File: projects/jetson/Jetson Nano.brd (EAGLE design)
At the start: 120 x 100 mm, 20 parts

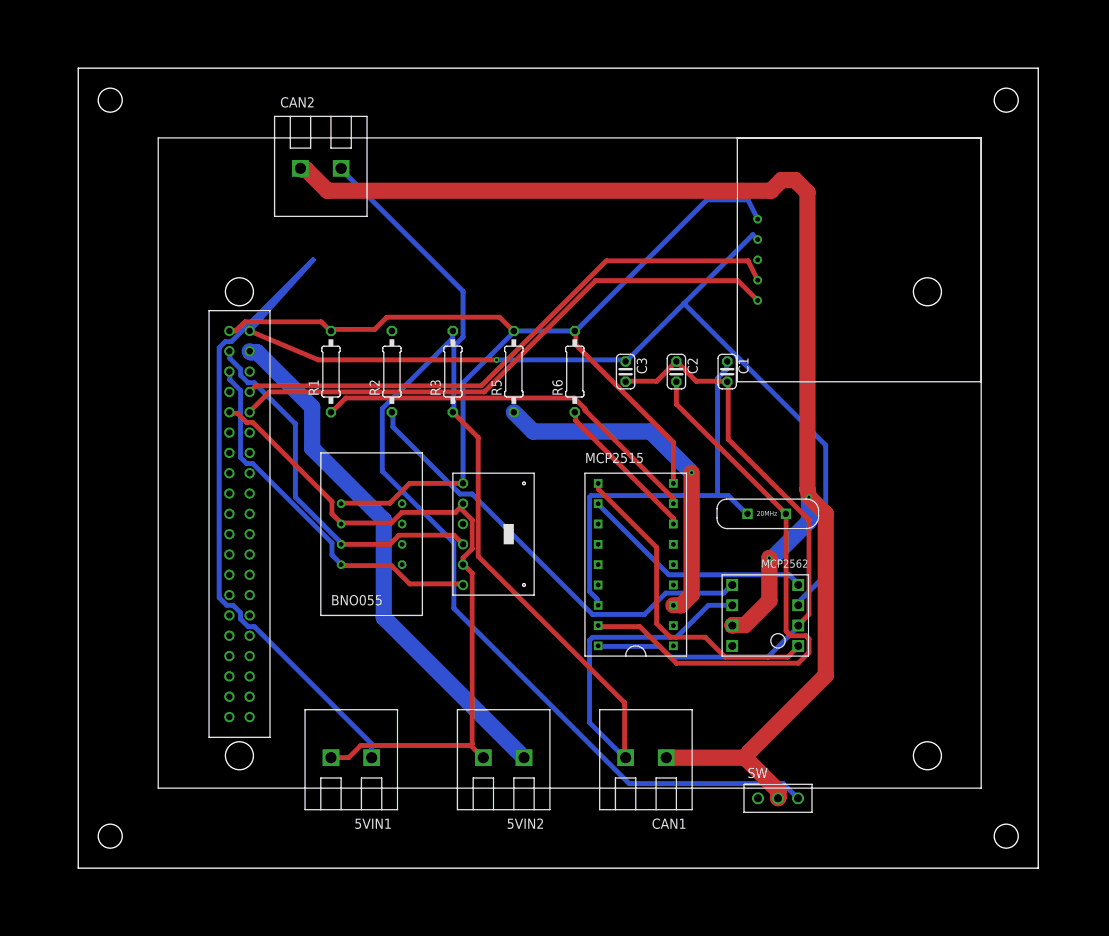
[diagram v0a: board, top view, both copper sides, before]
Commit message: Autoroute Jetson Board
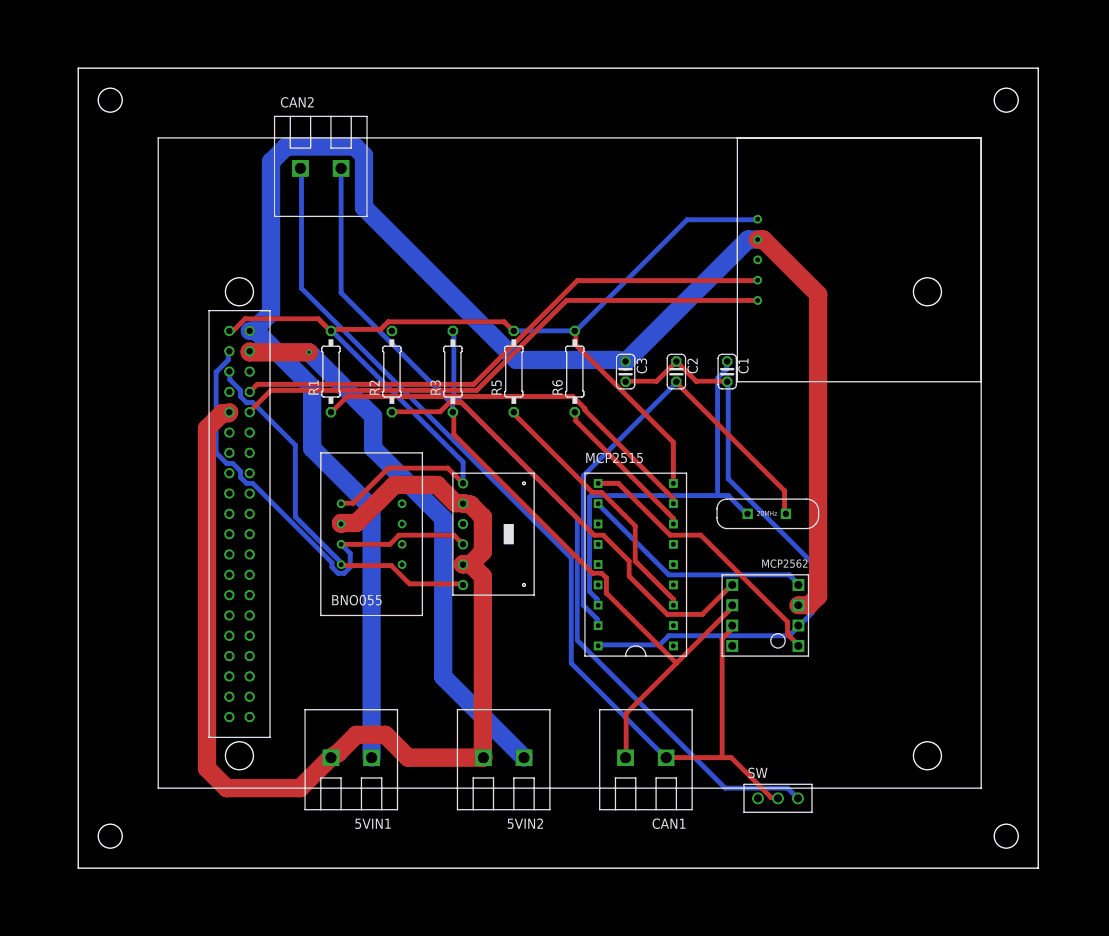
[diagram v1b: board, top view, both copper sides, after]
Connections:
- net +5V renamed +5V_1
- net N$2 renamed GND_1
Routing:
- net CAN_H2: track 179.2 -> 125.7 mm, vias 2 -> 0
- net GND_1: track 88.8 -> 139.4 mm
- net N$16: track 125.8 -> 104.6 mm
- net N$15: track 94.9 -> 80.9 mm
- net N$7: track 70.7 -> 58.4 mm
- net CAN_INT: track 43.4 -> 33.1 mm, vias 1 -> 0
- net N$3: track 46.7 -> 57.0 mm
- net +5V_1: track 205.9 -> 215.8 mm, vias 1 -> 0
- net N$8: track 40.7 -> 34.4 mm
- net 5V_2: track 65.5 -> 69.4 mm, vias 0 -> 1
- net +3V3: track 138.9 -> 142.2 mm
- net N$11: track 71.8 -> 69.3 mm
- net N$12: track 71.4 -> 69.3 mm
- net N$14: track 55.5 -> 56.6 mm
- net V-: track 77.4 -> 76.6 mm

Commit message: wakuwaku
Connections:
- removed net GND_1: 5VIN1.P$2, 5VIN2.P$2, JN1.GND-2, U$1.GND, U$1.SDO, U$2.2_GND
- removed net V-: C1.2, C2.1, C3.2, MCP1.VSS, U$4.VSS
- new net GND: 5VIN1.P$2, 5VIN2.P$2, C1.2, C2.1, C3.2, JN1.GND-2, MCP1.VSS, U$1.GND, U$1.SDO, U$2.2_GND, U$3.GND, U$4.VSS
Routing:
- net GND: track 0.00 -> 265.1 mm, vias 0 -> 1
- net GND_1: track 139.4 -> 0.00 mm
- net V-: track 76.6 -> 0.00 mm
- net N$8: track 34.4 -> 45.3 mm
- net N$3: track 57.0 -> 46.5 mm
- net CAN_H2: track 125.7 -> 136.0 mm
- net N$16: track 104.6 -> 113.6 mm
- net +5V_1: track 215.8 -> 207.7 mm
- net N$12: track 69.3 -> 75.7 mm, vias 0 -> 1
- net 5V_2: track 69.4 -> 66.5 mm, vias 1 -> 0
- net N$14: track 56.6 -> 54.5 mm
- net N$4: track 46.8 -> 48.6 mm
- net +3V3: track 142.2 -> 140.5 mm
- net N$13: track 49.6 -> 49.0 mm
- net N$7: track 58.4 -> 58.3 mm, vias 0 -> 1
- added copper zone on layer 1, net GND
- added copper zone on layer 16, net GND

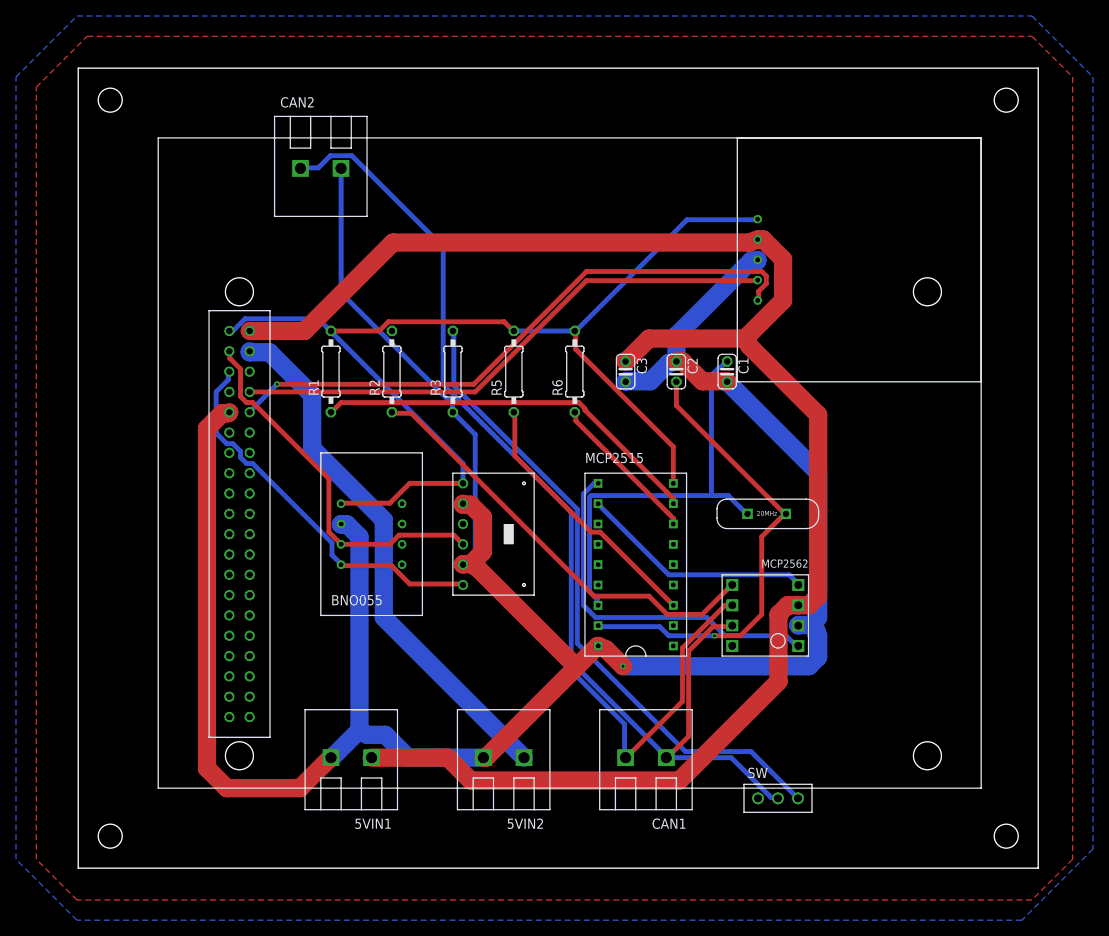
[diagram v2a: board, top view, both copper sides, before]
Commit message: Resize Jetson Board
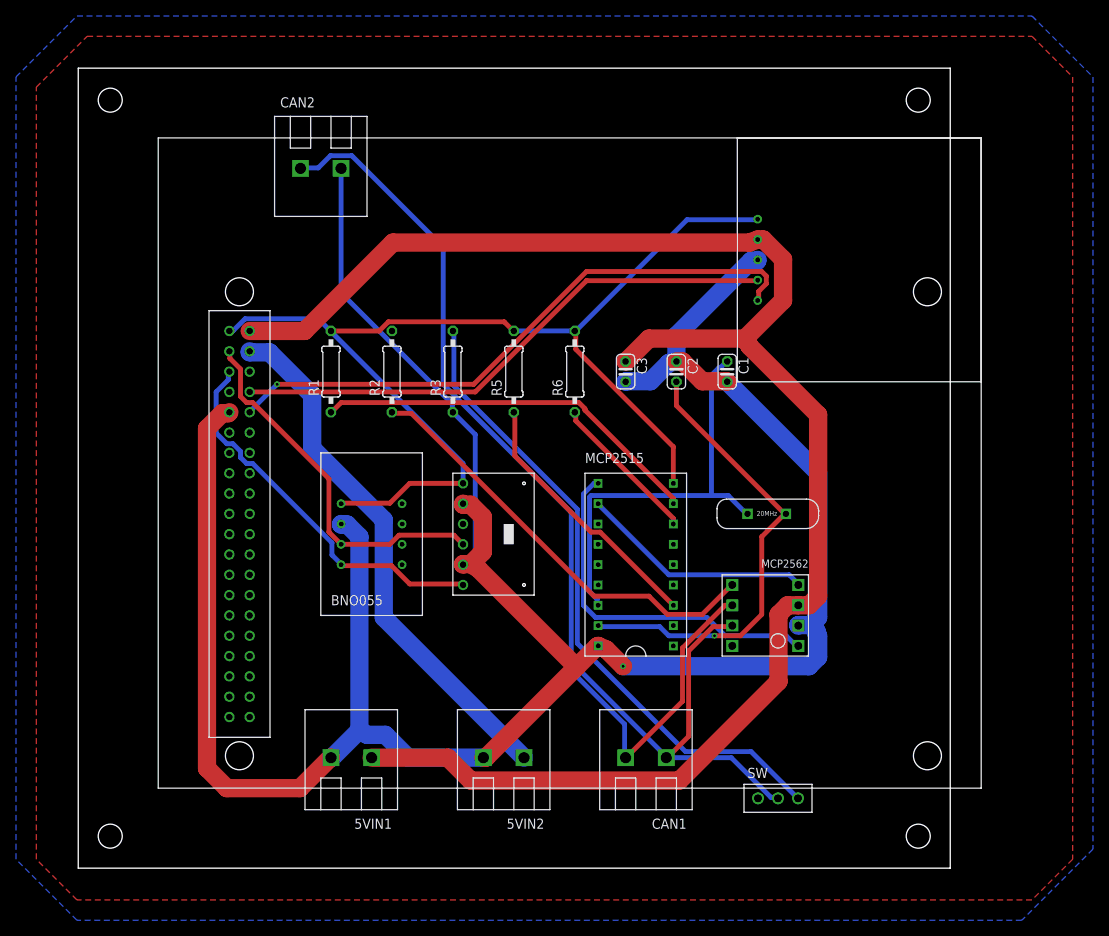
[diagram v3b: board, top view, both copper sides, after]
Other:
- board size 120 x 100 mm -> 109 x 100 mm
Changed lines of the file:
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@@
 <setting verticaltext="up"/>
 </settings>
-<grid distance="50" unitdist="mil" unit="mm" style="lines" multiple="1" display="no" altdistance="5" altunitdist="mil" altunit="mm"/>
+<grid distance="1" unitdist="mm" unit="mm" style="lines" multiple="1" display="no" altdistance="5" altunitdist="mil" altunit="mm"/>
 <layers>
 <layer number="1" name="Top" color="4" fill="1" visible="yes" active="yes"/>
@@
 <board>
 <plain>
-<wire x1="-10" y1="-10" x2="110" y2="-10" width="0" layer="20"/>
-<wire x1="110" y1="-10" x2="110" y2="90" width="0" layer="20"/>
-<wire x1="110" y1="90" x2="-10" y2="90" width="0" layer="20"/>
+<wire x1="-10" y1="-10" x2="99" y2="-10" width="0" layer="20"/>
+<wire x1="99" y1="-10" x2="99" y2="90" width="0" layer="20"/>
+<wire x1="99" y1="90" x2="-10" y2="90" width="0" layer="20"/>
 <wire x1="-10" y1="90" x2="-10" y2="-10" width="0" layer="20"/>
 <hole x="-6" y="86" drill="3"/>
-<hole x="106" y="86" drill="3"/>
-<hole x="106" y="-6" drill="3"/>
+<hole x="95" y="86" drill="3"/>
+<hole x="95" y="-6" drill="3"/>
 <hole x="-6" y="-6" drill="3"/>
 <hole x="10.15" y="4.05" drill="3.5"/>

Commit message: finish
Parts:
- moved JN1 2.00 mm to (6.89, 8.89)
- moved 5VIN1 2.00 mm to (22.1, 3.81)
- moved 5VIN2 2.00 mm to (41.2, 3.81)
- moved C1 2.00 mm to (69.1, 52.1)
- moved C3 2.00 mm to (56.4, 52.1)
- moved CAN1 2.00 mm to (59.0, 3.81)
- moved CAN2 2.00 mm to (18.3, 77.5)
- moved MCP1 2.00 mm to (57.7, 27.9)
- moved R1 2.00 mm to (19.6, 52.1)
- moved R2 2.00 mm to (27.2, 52.1)
- moved R3 2.00 mm to (34.8, 52.1)
- moved R5 2.00 mm to (42.5, 52.1)
- moved R6 2.00 mm to (50.1, 52.1)
- moved SW 2.00 mm to (75.5, -1.27)
- moved U$1 2.00 mm to (36.1, 39.4)
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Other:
- board size 109 x 100 mm -> 100 x 100 mm
